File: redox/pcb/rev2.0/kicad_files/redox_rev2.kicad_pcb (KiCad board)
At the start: 2 copper layers, 162.2 x 138.8 mm, 148 parts, among them J1 AVR-ISP-6, J2 OLED-SSD1306, K1 KEYSW, K10 KEYSW, K11 KEYSW, K12 KEYSW, K13 KEYSW, K14 KEYSW, K15 KEYSW, K16 KEYSW, K17 KEYSW, K18 KEYSW, K19 KEYSW, K2 KEYSW, K20 KEYSW, K21 KEYSW, K22 KEYSW, K23 KEYSW, K24 KEYSW, K25 KEYSW, K26 KEYSW, K27 KEYSW, K28 KEYSW, K29 KEYSW, K3 KEYSW, K30 KEYSW, K31 KEYSW, K32 KEYSW, K33 KEYSW, K34 KEYSW, K35 KEYSW, K4 KEYSW, K5 KEYSW, K6 KEYSW, K7 KEYSW, K8 KEYSW, K9 KEYSW, Q1 2N7002, U1 PRTR5V0U2X, U2 ATmega32U4-MU, Y1 16Mhz

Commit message: PCB Routing in progress
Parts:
- added USB2: HRO-TYPE-C-31-M-12, Keebio-Parts:HRO-TYPE-C-31-M-12-Assembly, F.Cu at (170.2, 41.4)
- C5: footprint Keebio-Parts:C_0603 -> Capacitor_Tantalum_SMD:CP_EIA-3216-12_Kemet-S_Pad1.58x1.35mm_HandSolder
- D1, D10, D11, D12, D13, D14, D15, D16, D17, D18, D19, D2, D20, D21, D22, D23, D24, D25, D26, D27, D28, D29, D3, D30, D31, D32, D33, D34, D35, D4, D5, D6, D7, D8, D9: footprint redox_footprints:Diode_SOD123 -> redox_footprints:D_0805_dualsided
- F1: footprint Keebio-Parts:Fuse_0805 -> Fuse:Fuse_1206_3216Metric_Pad1.42x1.75mm_HandSolder
- K11: footprint redox_footprints:Mx_Alps_125-dualside_with_LED -> redox_footprints:Mx_Alps_100-dualside_with_LED
- R10, R11, R12, R13, R14, R15, R16, R17, R18, R19, R20, R21, R22, R23, R24, R25, R26, R27, R28, R29, R30, R31, R32, R33, R34, R35, R36, R37, R38, R39, R40, R41, R42, R43, R44: footprint Keebio-Parts:Resistor-Compact -> redox_footprints:R_0805_dualsided
- U2: value ATmega32U4-MU -> ATmega32U4
- moved C7 92.2 mm to (184.8, 50.7), turned to 180 degrees
- moved C6 90.3 mm to (184.8, 52.5), turned to 180 degrees
- moved C5 83.8 mm to (180.1, 52.5), turned to 180 degrees
- moved QMK_BOTTOM 51.0 mm to (152.2, 46.7)
- moved QMK_FRONT 51.0 mm to (152.2, 46.7)
- moved RST_SW1 17.3 mm to (98.0, 44.5), turned to 270 degrees
- moved R34 15.5 mm to (180.6, 146.7)
- moved R43 15.1 mm to (231.1, 143.1)
- moved H2 14.9 mm to (92.5, 53.1)
- moved R40 14.7 mm to (213.5, 77.6), turned to 270 degrees
- moved R42 14.3 mm to (214.7, 133.4)
- moved D29 13.7 mm to (183.9, 125.5), turned to 90 degrees
- moved D3 13.7 mm to (86.1, 109.0), turned to 90 degrees
- moved D22 13.6 mm to (164.9, 85.5), turned to 90 degrees
- moved D8 13.6 mm to (107.7, 109.0), turned to 90 degrees
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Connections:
- net Net-(C1-Pad1) renamed XTAL1
- net Net-(C2-Pad1) renamed XTAL2
- C4 pad 1: Net-(C4-Pad1) -> GND
- C4 pad 2: GND -> Net-(C4-Pad2)
- C5 pad 1: GND -> +5V
- C5 pad 2: +5V -> GND
- JP5 pad 1: Net-(J2-Pad1) -> Net-(J2-Pad4)
- JP6 pad 1: Net-(J2-Pad2) -> Net-(J2-Pad3)
- JP7 pad 1: Net-(J2-Pad3) -> Net-(J2-Pad2)
- JP8 pad 1: Net-(J2-Pad4) -> Net-(J2-Pad1)
- K1 pad 3: Net-(K1-Pad3) -> +5V
- K1 pad 4: LEDGND -> Net-(K1-Pad4)
- K10 pad 3: Net-(K10-Pad3) -> +5V
- K10 pad 4: LEDGND -> Net-(K10-Pad4)
- K11 pad 3: Net-(K11-Pad3) -> +5V
- K11 pad 4: LEDGND -> Net-(K11-Pad4)
- K12 pad 3: Net-(K12-Pad3) -> +5V
- K12 pad 4: LEDGND -> Net-(K12-Pad4)
- K13 pad 3: Net-(K13-Pad3) -> +5V
- K13 pad 4: LEDGND -> Net-(K13-Pad4)
- K14 pad 3: Net-(K14-Pad3) -> +5V
- K14 pad 4: LEDGND -> Net-(K14-Pad4)
- K15 pad 3: Net-(K15-Pad3) -> +5V
- K15 pad 4: LEDGND -> Net-(K15-Pad4)
- K16 pad 3: Net-(K16-Pad3) -> +5V
- K16 pad 4: LEDGND -> Net-(K16-Pad4)
- K17 pad 3: Net-(K17-Pad3) -> +5V
- K17 pad 4: LEDGND -> Net-(K17-Pad4)
- K18 pad 3: Net-(K18-Pad3) -> +5V
- K18 pad 4: LEDGND -> Net-(K18-Pad4)
- K19 pad 3: Net-(K19-Pad3) -> +5V
- K19 pad 4: LEDGND -> Net-(K19-Pad4)
- K2 pad 3: Net-(K2-Pad3) -> +5V
- K2 pad 4: LEDGND -> Net-(K2-Pad4)
- K20 pad 3: Net-(K20-Pad3) -> +5V
- K20 pad 4: LEDGND -> Net-(K20-Pad4)
- K21 pad 3: Net-(K21-Pad3) -> +5V
- K21 pad 4: LEDGND -> Net-(K21-Pad4)
- K22 pad 3: Net-(K22-Pad3) -> +5V
- K22 pad 4: LEDGND -> Net-(K22-Pad4)
- K23 pad 3: Net-(K23-Pad3) -> +5V
- K23 pad 4: LEDGND -> Net-(K23-Pad4)
- K24 pad 3: Net-(K24-Pad3) -> +5V
- K24 pad 4: LEDGND -> Net-(K24-Pad4)
- K25 pad 3: Net-(K25-Pad3) -> +5V
- K25 pad 4: LEDGND -> Net-(K25-Pad4)
- K26 pad 3: Net-(K26-Pad3) -> +5V
- K26 pad 4: LEDGND -> Net-(K26-Pad4)
- K27 pad 3: Net-(K27-Pad3) -> +5V
- K27 pad 4: LEDGND -> Net-(K27-Pad4)
- K28 pad 3: Net-(K28-Pad3) -> +5V
- K28 pad 4: LEDGND -> Net-(K28-Pad4)
- K29 pad 3: Net-(K29-Pad3) -> +5V
- K29 pad 4: LEDGND -> Net-(K29-Pad4)
- K3 pad 3: Net-(K3-Pad3) -> +5V
- K3 pad 4: LEDGND -> Net-(K3-Pad4)
- K30 pad 3: Net-(K30-Pad3) -> +5V
- K30 pad 4: LEDGND -> Net-(K30-Pad4)
- K31 pad 3: Net-(K31-Pad3) -> +5V
- K31 pad 4: LEDGND -> Net-(K31-Pad4)
- K32 pad 3: Net-(K32-Pad3) -> +5V
- K32 pad 4: LEDGND -> Net-(K32-Pad4)
- K33 pad 3: Net-(K33-Pad3) -> +5V
- K33 pad 4: LEDGND -> Net-(K33-Pad4)
- K34 pad 3: Net-(K34-Pad3) -> +5V
- K34 pad 4: LEDGND -> Net-(K34-Pad4)
- K35 pad 3: Net-(K35-Pad3) -> +5V
- K35 pad 4: LEDGND -> Net-(K35-Pad4)
- K4 pad 3: Net-(K4-Pad3) -> +5V
- K4 pad 4: LEDGND -> Net-(K4-Pad4)
- K5 pad 3: Net-(K5-Pad3) -> +5V
- K5 pad 4: LEDGND -> Net-(K5-Pad4)
- K6 pad 3: Net-(K6-Pad3) -> +5V
- K6 pad 4: LEDGND -> Net-(K6-Pad4)
- K7 pad 3: Net-(K7-Pad3) -> +5V
- K7 pad 4: LEDGND -> Net-(K7-Pad4)
- K8 pad 3: Net-(K8-Pad3) -> +5V
- K8 pad 4: LEDGND -> Net-(K8-Pad4)
- K9 pad 3: Net-(K9-Pad3) -> +5V
- K9 pad 4: LEDGND -> Net-(K9-Pad4)
- R10 pad 1: Net-(K1-Pad3) -> LEDGND
- R10 pad 2: +5V -> Net-(K1-Pad4)
- R11 pad 1: Net-(K2-Pad3) -> LEDGND
- R11 pad 2: +5V -> Net-(K2-Pad4)
- R12 pad 1: Net-(K3-Pad3) -> LEDGND
- R12 pad 2: +5V -> Net-(K3-Pad4)
- R13 pad 1: Net-(K4-Pad3) -> LEDGND
- R13 pad 2: +5V -> Net-(K4-Pad4)
- R14 pad 1: Net-(K5-Pad3) -> LEDGND
- R14 pad 2: +5V -> Net-(K5-Pad4)
- R15 pad 1: Net-(K6-Pad3) -> LEDGND
- R15 pad 2: +5V -> Net-(K6-Pad4)
- R16 pad 1: Net-(K7-Pad3) -> LEDGND
- R16 pad 2: +5V -> Net-(K7-Pad4)
- R17 pad 1: Net-(K8-Pad3) -> LEDGND
- R17 pad 2: +5V -> Net-(K8-Pad4)
- R18 pad 1: Net-(K9-Pad3) -> LEDGND
- R18 pad 2: +5V -> Net-(K9-Pad4)
- R19 pad 1: Net-(K10-Pad3) -> LEDGND
- R19 pad 2: +5V -> Net-(K10-Pad4)
- R20 pad 1: Net-(K11-Pad3) -> LEDGND
- R20 pad 2: +5V -> Net-(K11-Pad4)
- R21 pad 1: Net-(K12-Pad3) -> LEDGND
- R21 pad 2: +5V -> Net-(K12-Pad4)
- R22 pad 1: Net-(K13-Pad3) -> LEDGND
- R22 pad 2: +5V -> Net-(K13-Pad4)
- R23 pad 1: Net-(K14-Pad3) -> LEDGND
- R23 pad 2: +5V -> Net-(K14-Pad4)
- R24 pad 1: Net-(K15-Pad3) -> LEDGND
- R24 pad 2: +5V -> Net-(K15-Pad4)
- R25 pad 1: Net-(K16-Pad3) -> LEDGND
- R25 pad 2: +5V -> Net-(K16-Pad4)
- R26 pad 1: Net-(K17-Pad3) -> LEDGND
- R26 pad 2: +5V -> Net-(K17-Pad4)
- R27 pad 1: Net-(K18-Pad3) -> LEDGND
- R27 pad 2: +5V -> Net-(K18-Pad4)
- R28 pad 1: Net-(K19-Pad3) -> LEDGND
- R28 pad 2: +5V -> Net-(K19-Pad4)
- R29 pad 1: Net-(K20-Pad3) -> LEDGND
- R29 pad 2: +5V -> Net-(K20-Pad4)
- R30 pad 1: Net-(K21-Pad3) -> LEDGND
- R30 pad 2: +5V -> Net-(K21-Pad4)
- R31 pad 1: Net-(K22-Pad3) -> LEDGND
- R31 pad 2: +5V -> Net-(K22-Pad4)
- R32 pad 1: Net-(K23-Pad3) -> LEDGND
- R32 pad 2: +5V -> Net-(K23-Pad4)
- R33 pad 1: Net-(K24-Pad3) -> LEDGND
- R33 pad 2: +5V -> Net-(K24-Pad4)
- R34 pad 1: Net-(K25-Pad3) -> LEDGND
- R34 pad 2: +5V -> Net-(K25-Pad4)
- R35 pad 1: Net-(K26-Pad3) -> LEDGND
- R35 pad 2: +5V -> Net-(K26-Pad4)
- R36 pad 1: Net-(K27-Pad3) -> LEDGND
- R36 pad 2: +5V -> Net-(K27-Pad4)
- R37 pad 1: Net-(K28-Pad3) -> LEDGND
- R37 pad 2: +5V -> Net-(K28-Pad4)
- R38 pad 1: Net-(K29-Pad3) -> LEDGND
- R38 pad 2: +5V -> Net-(K29-Pad4)
- R39 pad 1: Net-(K30-Pad3) -> LEDGND
- R39 pad 2: +5V -> Net-(K30-Pad4)
- R40 pad 1: Net-(K31-Pad3) -> LEDGND
- R40 pad 2: +5V -> Net-(K31-Pad4)
- R41 pad 1: Net-(K32-Pad3) -> LEDGND
- R41 pad 2: +5V -> Net-(K32-Pad4)
- R42 pad 1: Net-(K33-Pad3) -> LEDGND
- R42 pad 2: +5V -> Net-(K33-Pad4)
- R43 pad 1: Net-(K34-Pad3) -> LEDGND
- R43 pad 2: +5V -> Net-(K34-Pad4)
- R44 pad 1: Net-(K35-Pad3) -> LEDGND
- R44 pad 2: +5V -> Net-(K35-Pad4)
- U2 pad 1: (no net) -> col0
- U2 pad 20: rgb_data -> (no net)
- U2 pad 21: col6 -> (no net)
- U2 pad 22: col5 -> (no net)
- U2 pad 27: col4 -> rgb_data
- U2 pad 28: col3 -> col6
- U2 pad 29: col2 -> col5
- U2 pad 30: (no net) -> col4
- U2 pad 31: (no net) -> col3
- U2 pad 32: row4 -> col2
- U2 pad 36: row3 -> row0
- U2 pad 37: row2 -> col1
- U2 pad 39: row0 -> row2
- U2 pad 40: col1 -> row3
- U2 pad 41: col0 -> row4
- U2 pad 45: GND -> (no net)
- U2 pad 6: Net-(C4-Pad1) -> Net-(C4-Pad2)
- U2 pad 7: +5V -> VCC
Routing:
- net LEDGND: track 0.00 -> 811.0 mm
- net row4: track 0.00 -> 266.6 mm
- net row3: track 0.00 -> 238.8 mm
- net row2: track 0.00 -> 215.3 mm
- net row1: track 0.00 -> 178.4 mm
- net row0: track 0.00 -> 165.7 mm
- net col1: track 0.00 -> 117.3 mm
- net col6: track 0.00 -> 112.9 mm
- net col0: track 0.00 -> 92.5 mm
- net col4: track 0.00 -> 77.9 mm, vias 0 -> 1
- net col2: track 0.00 -> 71.6 mm
- net col3: track 0.00 -> 71.6 mm
- net +5V: track 0.00 -> 60.7 mm, vias 0 -> 4
- net col5: track 0.00 -> 53.7 mm
- net VCC: track 0.00 -> 41.9 mm
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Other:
- outline, holes or cut-outs redrawn
- net class +5V: trace_width 0.5 -> 0.3
- net class Default: trace_width 0.25 -> 0.2
- net class GND: trace_width 0.4 -> 0.3
- net class VCC: trace_width 0.5 -> 0.3

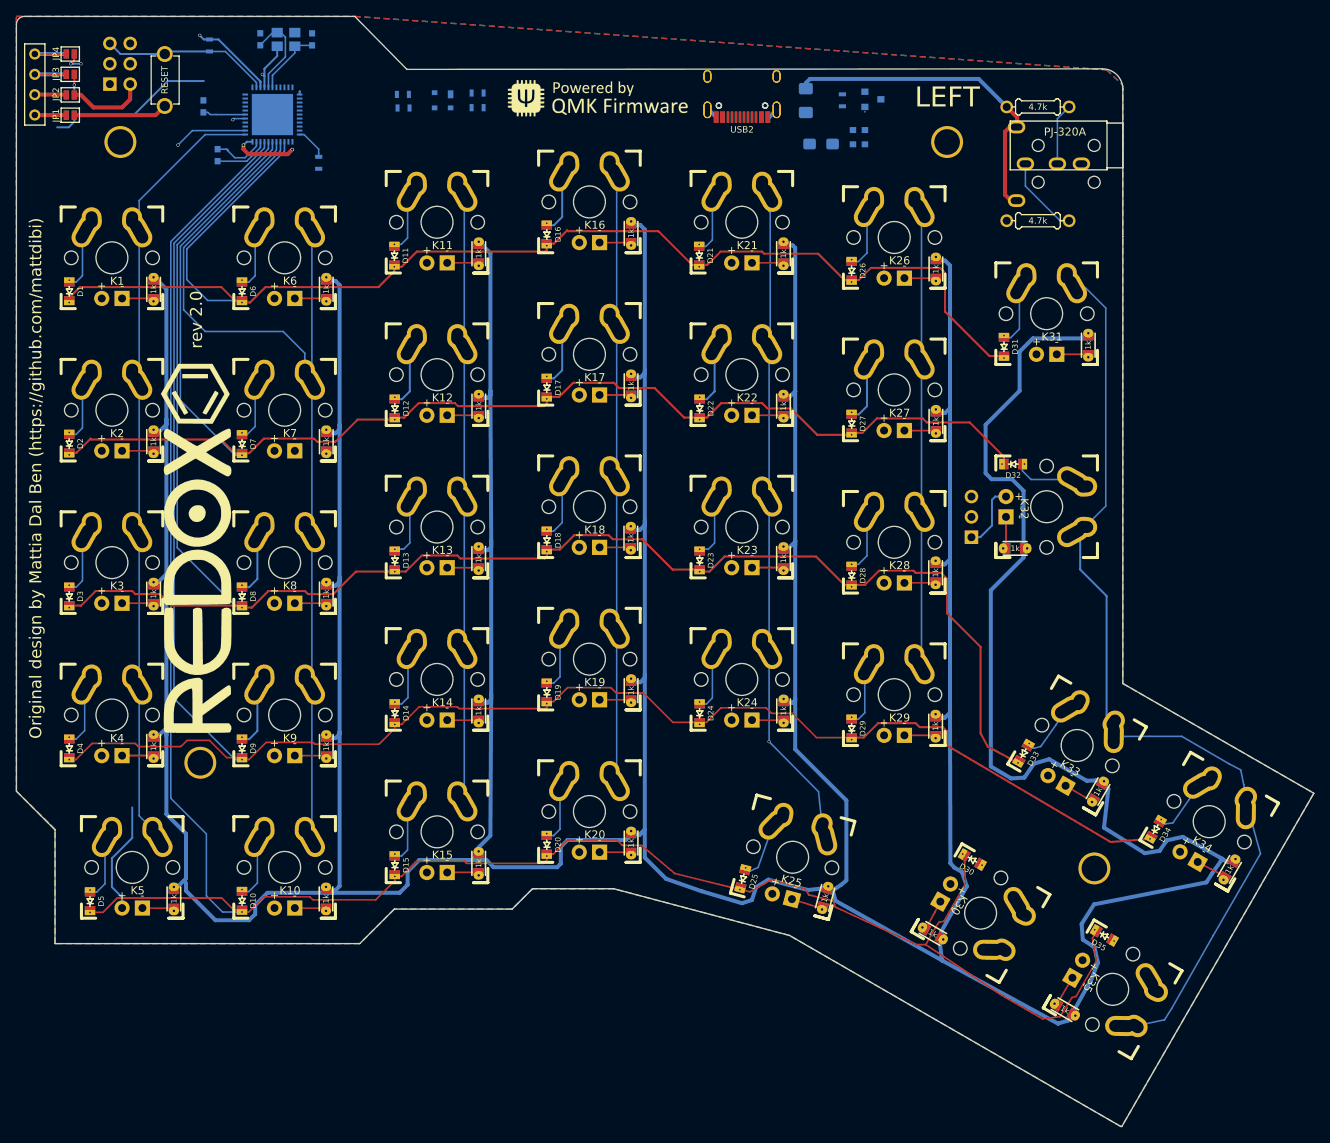
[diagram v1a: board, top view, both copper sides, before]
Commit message: Create dual sided usb
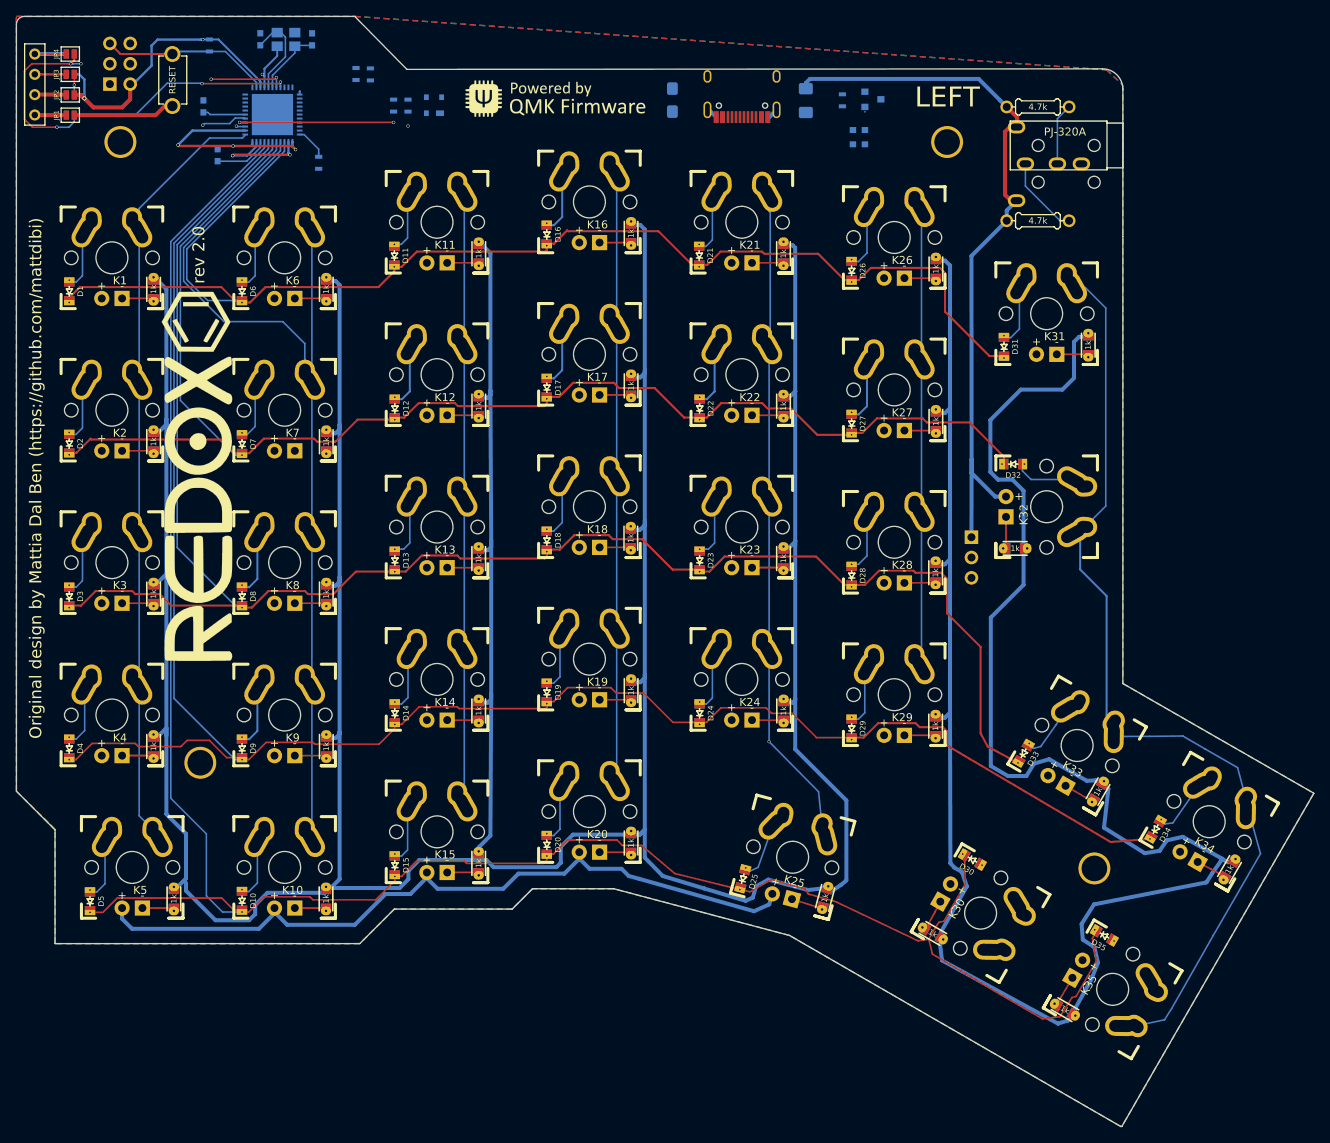
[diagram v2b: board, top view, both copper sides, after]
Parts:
- removed USB2: HRO-TYPE-C-31-M-12, Keebio-Parts:HRO-TYPE-C-31-M-12-Assembly
- USB1: footprint Keebio-Parts:HRO-TYPE-C-31-M-12-Assembly -> redox_footprints:HRO-TYPE-C-31-M-12-Assembly_dualsided
- moved C5 19.4 mm to (161.5, 47.0), turned to 270 degrees
- moved R2 15.4 mm to (122.0, 43.7), turned to 90 degrees
- moved R1 14.0 mm to (123.8, 43.8), turned to 90 degrees
- moved REDOX_BOTTOM 9.00 mm to (102.2, 94.0)
- moved REDOX_FRONT 9.00 mm to (102.2, 94.0)
- moved QMK_BOTTOM 5.30 mm to (146.9, 46.8)
- moved QMK_FRONT 5.30 mm to (146.9, 46.8)
- moved R3 1.82 mm to (126.7, 47.6), turned to 90 degrees
- moved U1 1.24 mm to (131.7, 47.6), turned to 180 degrees
- moved RST_SW1 0.96 mm to (99.0, 44.5)
- moved R4 0.64 mm to (128.4, 47.6), turned to 90 degrees
- turned RGB_STRIP1 to 180 degrees
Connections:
- K1 pad 3: +5V -> VCC
- K10 pad 3: +5V -> VCC
- K11 pad 3: +5V -> VCC
- K12 pad 3: +5V -> VCC
- K13 pad 3: +5V -> VCC
- K14 pad 3: +5V -> VCC
- K15 pad 3: +5V -> VCC
- K16 pad 3: +5V -> VCC
- K17 pad 3: +5V -> VCC
- K18 pad 3: +5V -> VCC
- K19 pad 3: +5V -> VCC
- K2 pad 3: +5V -> VCC
- K20 pad 3: +5V -> VCC
- K21 pad 3: +5V -> VCC
- K22 pad 3: +5V -> VCC
- K23 pad 3: +5V -> VCC
- K24 pad 3: +5V -> VCC
- K25 pad 3: +5V -> VCC
- K26 pad 3: +5V -> VCC
- K27 pad 3: +5V -> VCC
- K28 pad 3: +5V -> VCC
- K29 pad 3: +5V -> VCC
- K3 pad 3: +5V -> VCC
- K30 pad 3: +5V -> VCC
- K31 pad 3: +5V -> VCC
- K32 pad 3: +5V -> VCC
- K33 pad 3: +5V -> VCC
- K34 pad 3: +5V -> VCC
- K35 pad 3: +5V -> VCC
- K4 pad 3: +5V -> VCC
- K5 pad 3: +5V -> VCC
- K6 pad 3: +5V -> VCC
- K7 pad 3: +5V -> VCC
- K8 pad 3: +5V -> VCC
- K9 pad 3: +5V -> VCC
- RGB_STRIP1 pad 1: +5V -> VCC
- U2 pad 12: Net-(R9-Pad2) -> (no net)
- U2 pad 26: (no net) -> rgb_data
- U2 pad 27: rgb_data -> col6
- U2 pad 28: col6 -> col5
- U2 pad 29: col5 -> col4
- U2 pad 30: col4 -> Net-(R9-Pad2)
- USB1 pad 3: (no net) -> Net-(USB1-Pad3)
- USB1 pad 9: (no net) -> Net-(USB1-Pad9)
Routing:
- net VCC: track 41.9 -> 189.6 mm
- net SDA: track 31.6 -> 58.5 mm, vias 2 -> 5
- net LEDGND: track 811.0 -> 790.6 mm
- net D+: track 0.00 -> 20.0 mm, vias 0 -> 2
- net GND: track 29.5 -> 40.2 mm, vias 2 -> 4
- net SCL: track 12.6 -> 22.1 mm, vias 1 -> 3
- net +5V: track 60.7 -> 65.5 mm, vias 4 -> 5
- net col1: track 117.3 -> 115.9 mm
- net D-: track 0.00 -> 1.13 mm, vias 0 -> 2
- net col0: track 92.5 -> 91.9 mm

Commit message: Routing almost finished
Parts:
- moved R2 54.9 mm to (176.8, 45.4), turned to 270 degrees
- moved Q1 47.8 mm to (138.8, 47.8), turned to 270 degrees
- moved R9 47.1 mm to (135.7, 47.5)
- moved QMK_BOTTOM 42.6 mm to (189.5, 46.4)
- moved QMK_FRONT 42.6 mm to (189.5, 46.4)
- moved R1 40.1 mm to (163.8, 45.3), turned to 270 degrees
- moved C7 31.5 mm to (153.6, 46.3), turned to 90 degrees
- moved C6 30.3 mm to (155.2, 46.3), turned to 90 degrees
- moved F1 13.6 mm to (165.3, 51.5), turned to 0 degrees
- moved C5 3.55 mm to (157.9, 47.0)
- moved C1 1.59 mm to (115.0, 40.0)
- moved C2 1.51 mm to (108.7, 40.1)
- moved Y1 1.50 mm to (111.9, 40.1)
- moved C4 1.28 mm to (104.2, 47.8)
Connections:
- U2 pad 26: rgb_data -> Net-(R9-Pad2)
- U2 pad 28: col5 -> rgb_data
- U2 pad 29: col4 -> col5
- U2 pad 30: Net-(R9-Pad2) -> col4
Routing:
- net VCC: track 189.6 -> 952.1 mm, vias 0 -> 9
- net col5: track 53.7 -> 211.7 mm, vias 0 -> 1
- net col6: track 112.8 -> 246.1 mm, vias 0 -> 1
- net rgb_data: track 0.00 -> 130.6 mm, vias 0 -> 1
- net SCL: track 22.1 -> 141.9 mm, vias 3 -> 4
- net SDA: track 58.5 -> 158.0 mm
- net col4: track 77.9 -> 175.1 mm
- net col3: track 71.6 -> 148.4 mm, vias 0 -> 1
- net col2: track 71.6 -> 131.9 mm, vias 0 -> 1
- net Net-(R3-Pad2): track 0.00 -> 58.9 mm, vias 0 -> 2
- net Net-(R4-Pad2): track 0.00 -> 53.8 mm, vias 0 -> 2
- net LEDGND: track 790.6 -> 825.6 mm
- net D-: track 1.13 -> 27.1 mm
- net Net-(R9-Pad2): track 0.00 -> 24.7 mm, vias 0 -> 2
- net MISO: track 0.00 -> 19.7 mm
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
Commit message: PCB finished for rev2.0
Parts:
- moved C3 0.36 mm to (104.7, 54.2)
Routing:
- net +5V: track 70.6 -> 141.3 mm, vias 4 -> 7
- net GND: track 43.8 -> 96.8 mm
- net VCC: track 952.1 -> 955.6 mm, vias 9 -> 8
- net SDA: track 158.0 -> 157.5 mm
- net Net-(R4-Pad2): track 53.8 -> 53.6 mm, vias 2 -> 3
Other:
- board text added: "GND"
- board text added: "SCL"
- board text added: "SDA"
- board text added: "VCC"

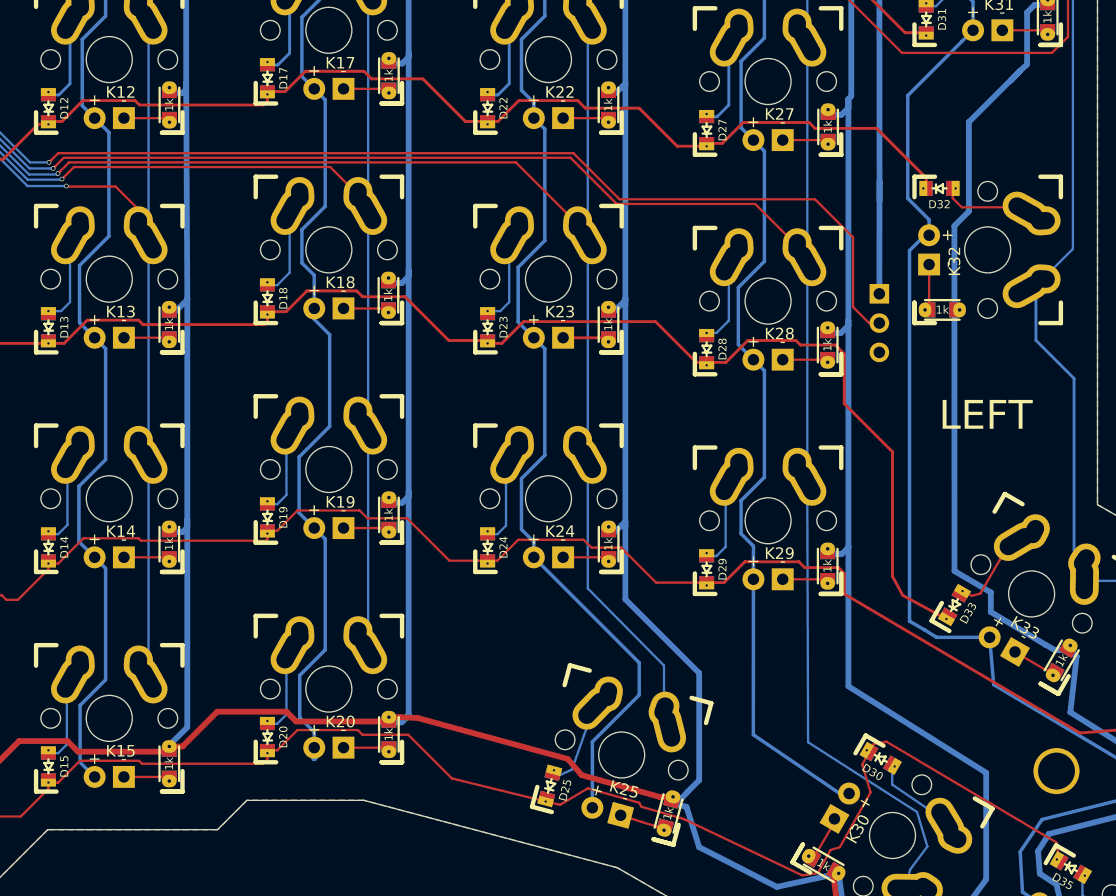
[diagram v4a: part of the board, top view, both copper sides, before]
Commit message: Add OSH logo
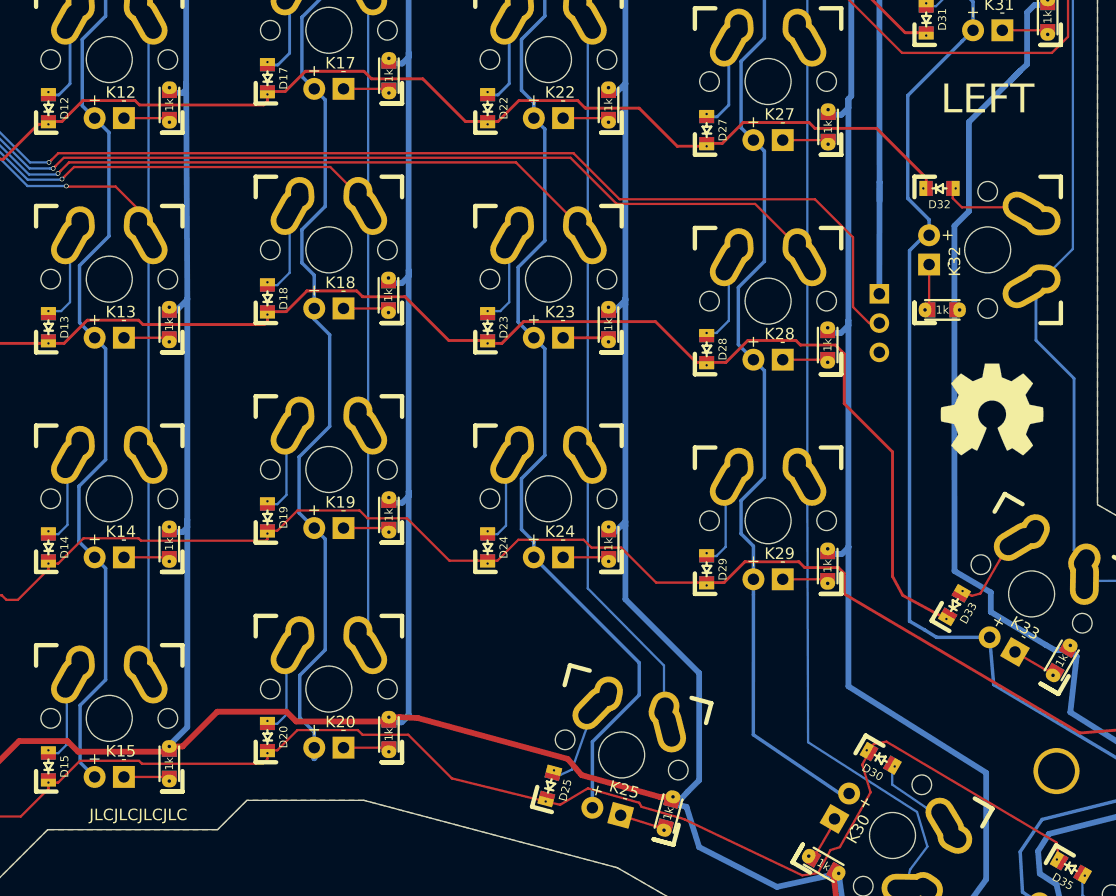
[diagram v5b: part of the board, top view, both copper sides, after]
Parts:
- added REF***: OSHW-Logo2_14.6x12mm_SilkScreen, redox_footprints:OSHW-Symbol_8.9x8mm_SilkScreen, B.Cu at (208.7, 111.7)
- added REF***: OSHW-Logo2_14.6x12mm_SilkScreen, redox_footprints:OSHW-Symbol_8.9x8mm_SilkScreen, F.Cu at (208.7, 111.7)
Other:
- board text added: "JLCJLCJLCJLC"
